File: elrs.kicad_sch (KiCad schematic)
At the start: 35 parts, among them J10 5V, J11 5V, J12 5V, J26 5V, J31 5V, U12 WL9005D4-33, U19 XL-1010RGBC-WS2812B, U2 ESP32-C3FH4, U20 SX1281IMLTRT

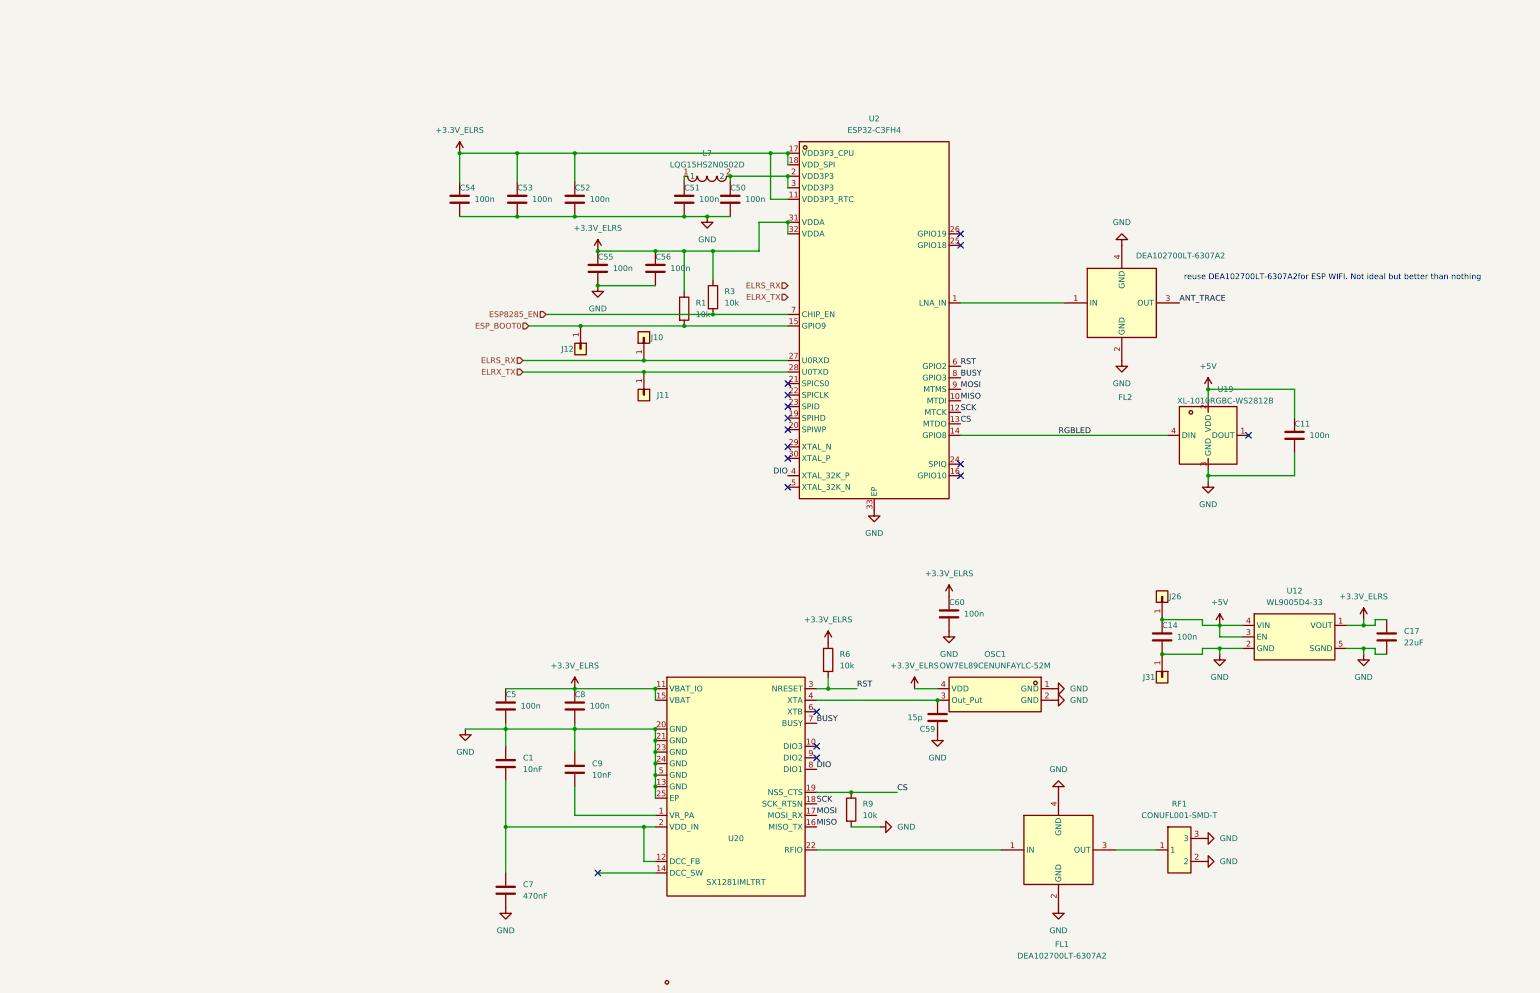
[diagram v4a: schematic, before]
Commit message: Switched to RP2354B for V2 of the FC for more IO. I want to try implement OSD on PIO state machine. I know BF already uses all of them but it should be possible and then later try to combine it witht the WS2812 protocol PIO2. If anybody here has any experience with analog OSD generation let me know, I just want to make a circuit that would allow further software development later. The reason I want to do it this way is it's cheap BOM<1 euro and low footprint, just 2 2x2 IC's and some passives.
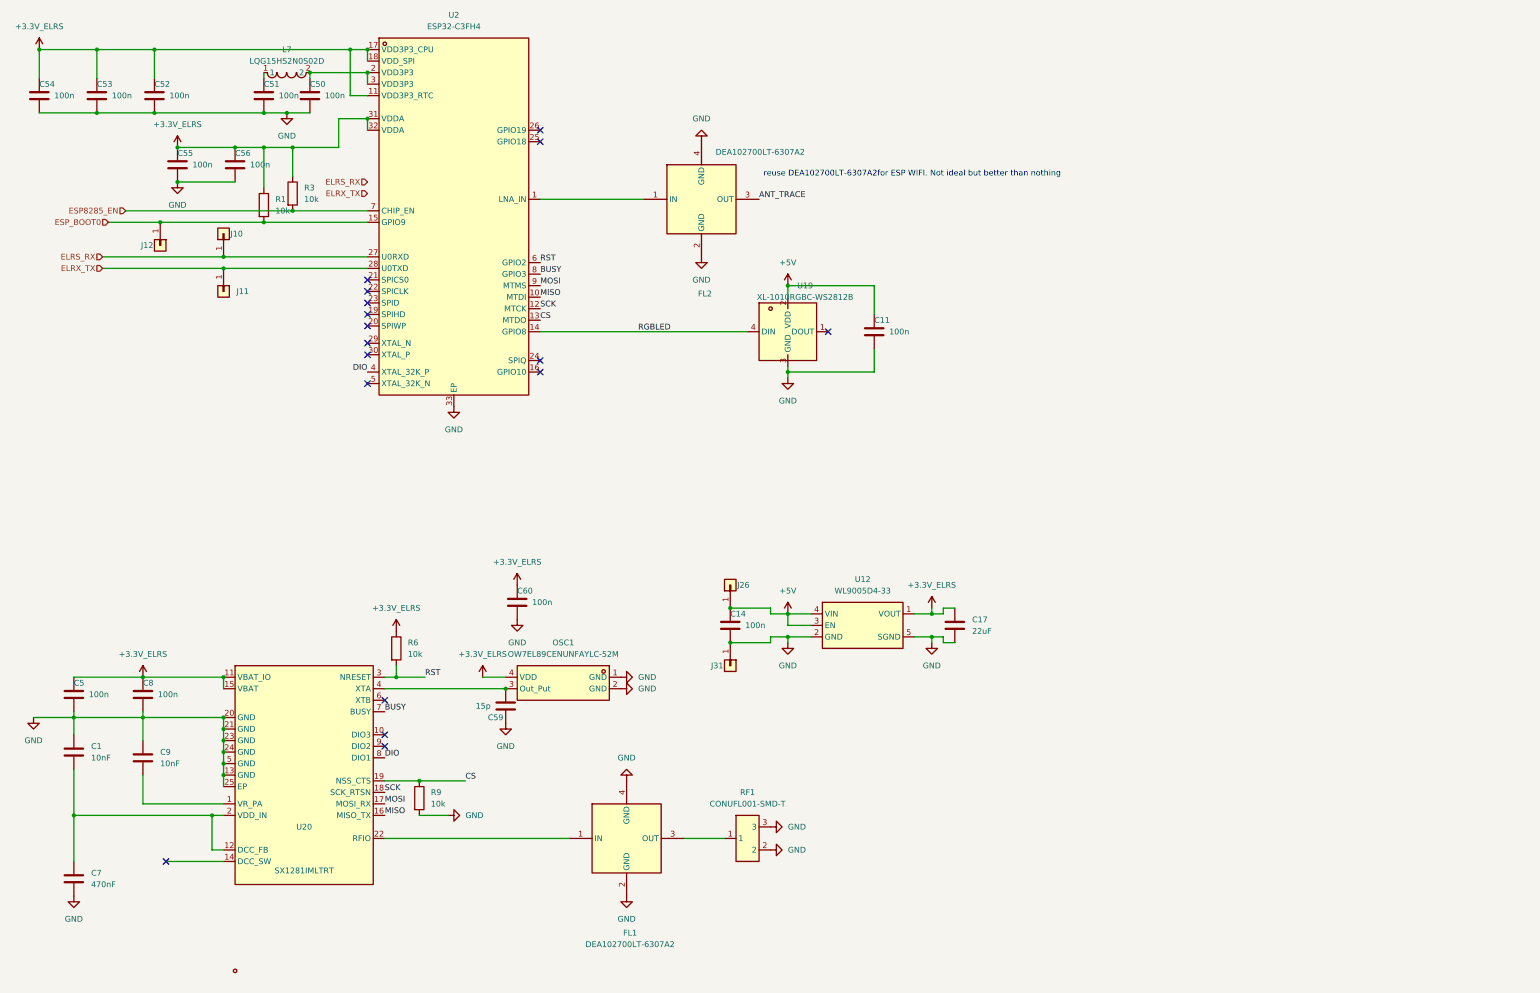
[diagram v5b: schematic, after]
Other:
- moved on the sheet: C1, C11, C14, C17, C5, C50, C51, C52, C53, C54, C55, C56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
